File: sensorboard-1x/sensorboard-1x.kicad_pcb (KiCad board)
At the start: 2 copper layers, 11.5 x 42.5 mm, 8 parts, among them J1 Conn_02x02_Odd_Even, U1 CNY70

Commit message: shrunk the sensorboard slightly, removed extra mounting hole.
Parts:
- removed H2: MountingHole, Mounting_Holes:MountingHole_3.2mm_M3
- moved Cath1 0.47 mm to (152.8, 87.8)
- moved Coll1 0.47 mm to (152.8, 87.8)
- moved An1 0.40 mm to (144.7, 87.8)
- moved Emit1 0.40 mm to (144.7, 87.8)
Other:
- board size 11.5 x 42.5 mm -> 10.4 x 29.1 mm

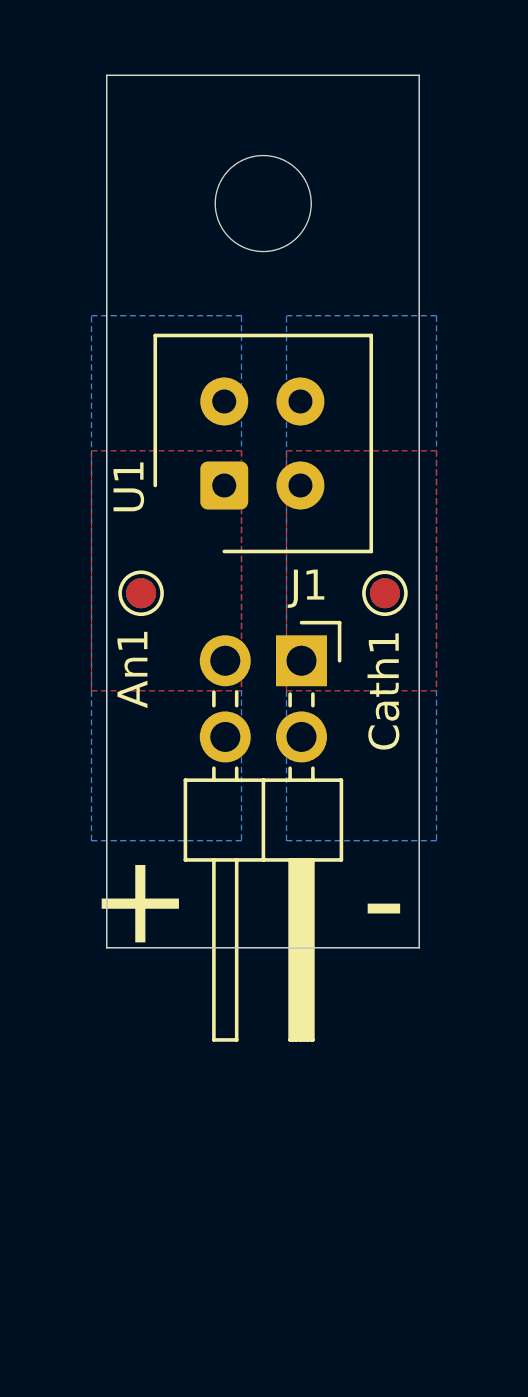
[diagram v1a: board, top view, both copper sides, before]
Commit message: Narrowed the board, better matching Cybrid's dimensions.
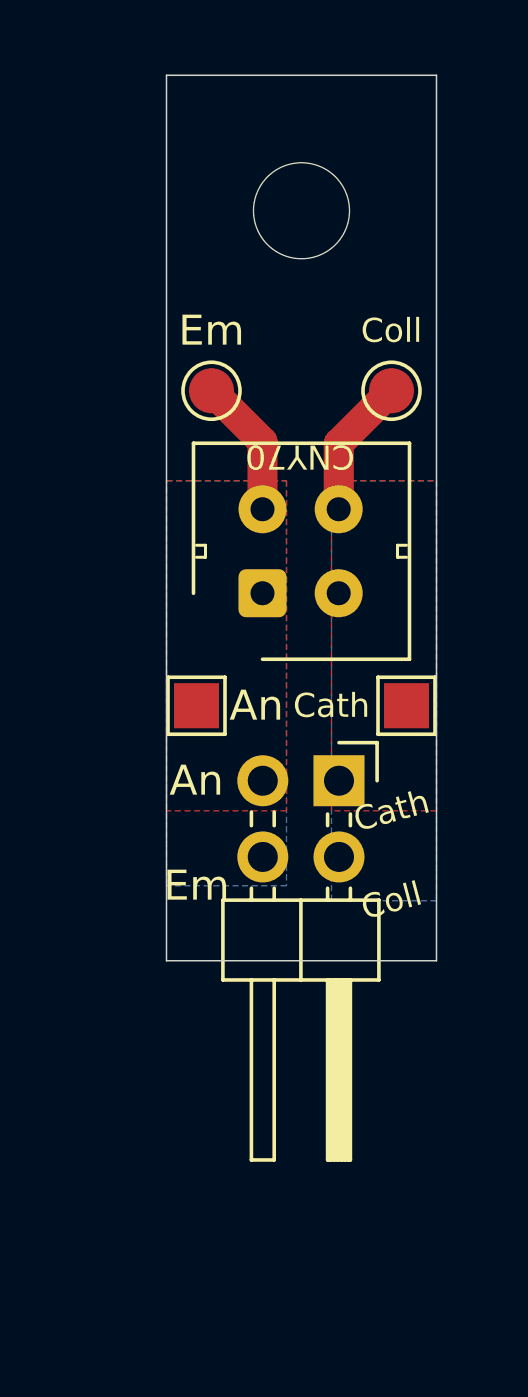
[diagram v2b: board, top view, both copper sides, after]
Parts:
- An1, Cath1: footprint TestPoint:TestPoint_Pad_D1.0mm -> TestPoint:TestPoint_Pad_1.5x1.5mm
- Coll1, Emit1: footprint TestPoint:TestPoint_Pad_D1.0mm -> TestPoint:TestPoint_Pad_D1.5mm; moved to F.Cu
- moved Emit1 7.15 mm to (147.0, 81.0)
- moved Coll1 6.75 mm to (153.0, 81.0)
- moved J1 4.19 mm to (151.2, 94.0)
- moved An1 4.18 mm to (146.5, 91.5)
- moved Cath1 3.82 mm to (153.5, 91.5)
- moved U1 3.81 mm to (148.7, 87.8)
- moved H1 1.30 mm to (150.0, 75.0)
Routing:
- net /Collector: track 0.00 -> 4.68 mm
- net /Emitter: track 0.00 -> 4.65 mm
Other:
- board size 10.4 x 29.1 mm -> 9 x 29.5 mm
- board text added: "An"
- board text added: "Cath"
- board text added: "Coll"
- board text added: "Em"
- board text removed: "+"
- board text removed: "-"

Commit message: Add/update board rev silkscreen, nothing else
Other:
- board text added: "jkominek piano-conversion sensor rev0"
